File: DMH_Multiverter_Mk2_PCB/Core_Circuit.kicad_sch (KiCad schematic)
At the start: 9 parts, among them U1 TL072

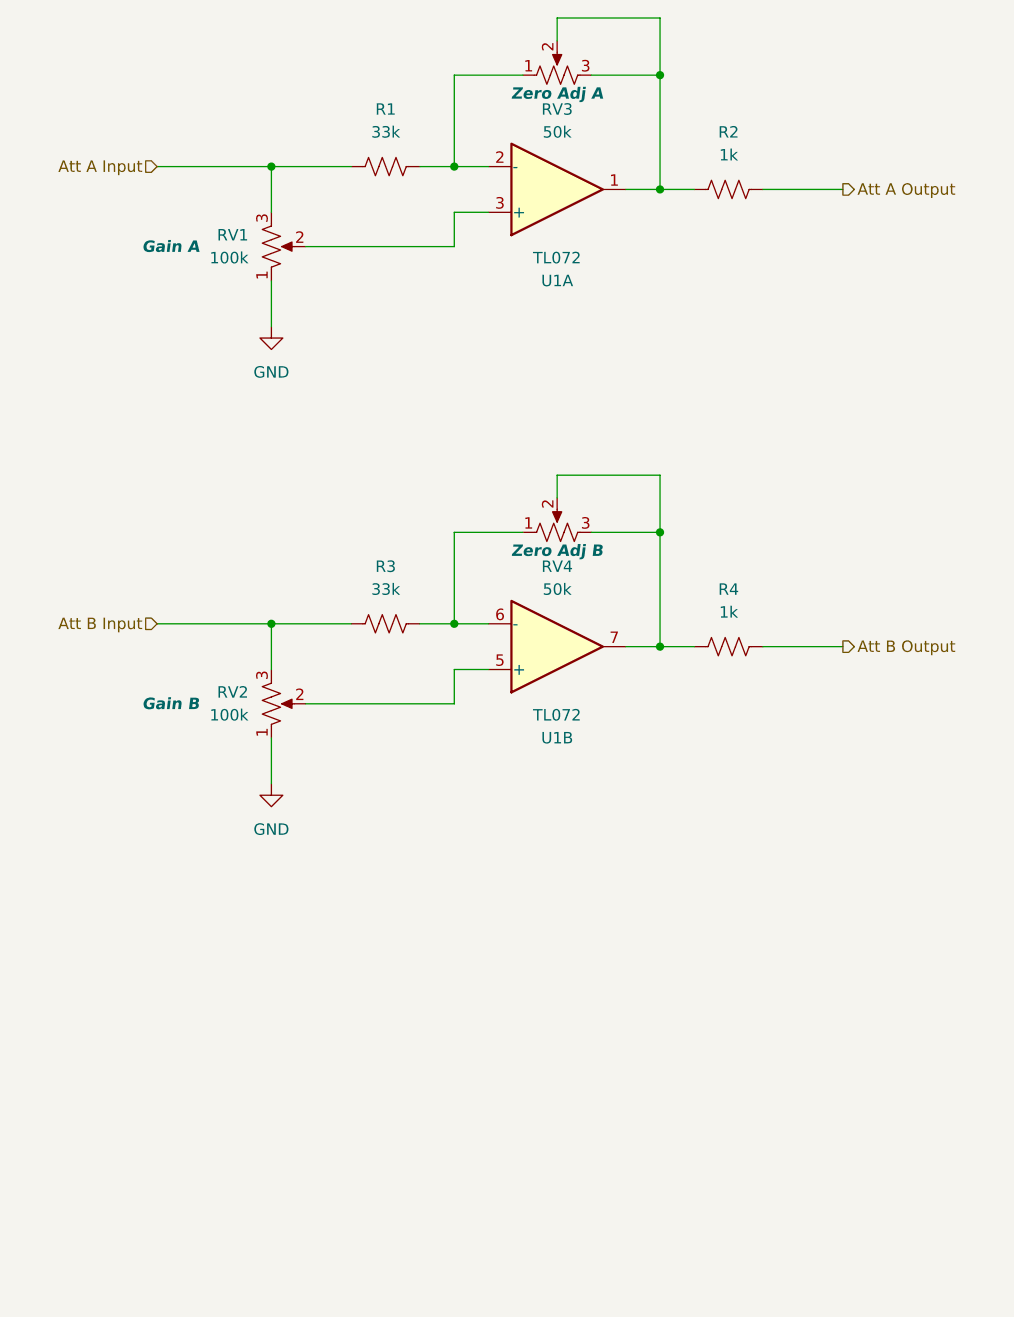
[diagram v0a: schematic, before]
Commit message: Added 3rd attenuverter to Panel and Schematic
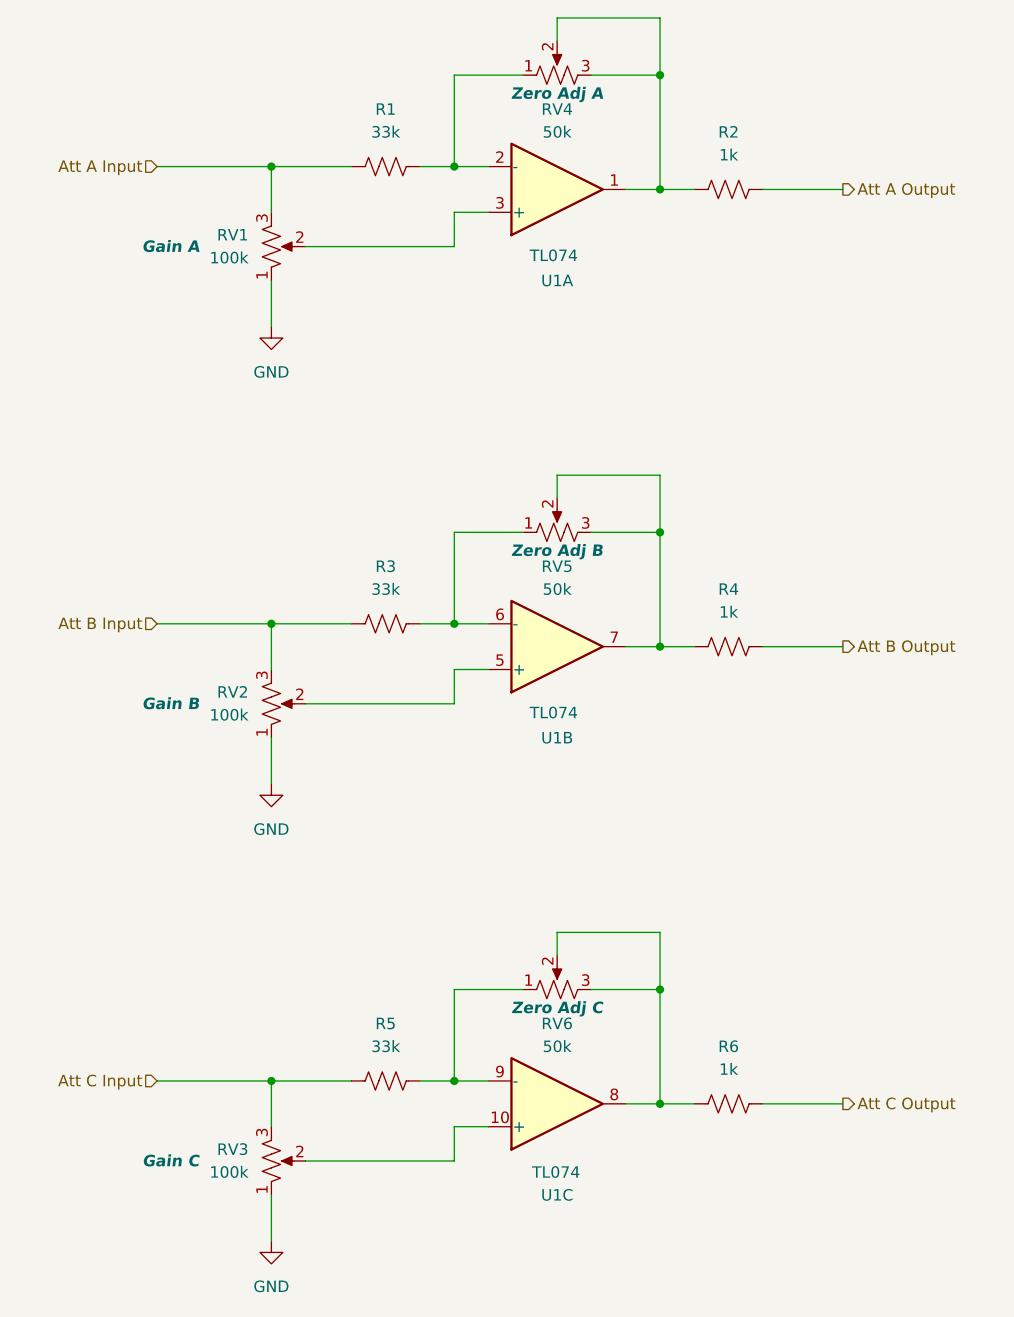
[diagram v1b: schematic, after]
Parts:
- added R5: 33k, Resistor_THT:R_Axial_DIN0207_L6.3mm_D2.5mm_P7.62mm_Horizontal, symbol Device:R_US
- added R6: 1k, Resistor_THT:R_Axial_DIN0207_L6.3mm_D2.5mm_P7.62mm_Horizontal, symbol Device:R_US
- added RV3: 100k, SynthStuff:Potentiometer_TT_P110KH1, symbol Device:R_Potentiometer_US
- added RV6: 50k, Potentiometer_THT:Potentiometer_Bourns_3296W_Vertical, symbol Device:R_Potentiometer_US
- added unit 3 of U1
- U1: value TL072 -> TL074; symbol Amplifier_Operational:TL072 -> Amplifier_Operational:TL074
- renumbered RV3 to RV4, RV4 to RV5
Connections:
- net GND: now also RV3.1
- new net: R5.2, RV6.1, U1.9 (-)
- new net: RV3.2, U1.10 (+)
- new net: R6.1, RV6.2, RV6.3, U1.8
- new net Att C Input: R5.1, RV3.3
- new net Att C Output: R6.2

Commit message: Main PCB components placed
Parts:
- U1: footprint Package_DIP:DIP-8_W7.62mm_Socket -> Package_DIP:DIP-14_W7.62mm_Socket
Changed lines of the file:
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@@
 			)
 		)
-		(property "Footprint" "Package_DIP:DIP-8_W7.62mm_Socket"
+		(property "Footprint" "Package_DIP:DIP-14_W7.62mm_Socket"
 			(at 74.93 40.64 0)
 			(effects
@@
 			)
 		)
-		(property "Footprint" "Package_DIP:DIP-8_W7.62mm_Socket"
+		(property "Footprint" "Package_DIP:DIP-14_W7.62mm_Socket"
 			(at 74.93 91.44 0)
 			(effects
@@
 			)
 		)
-		(property "Footprint" "Package_DIP:DIP-8_W7.62mm_Socket"
+		(property "Footprint" "Package_DIP:DIP-14_W7.62mm_Socket"
 			(at 74.93 142.24 0)
 			(effects
